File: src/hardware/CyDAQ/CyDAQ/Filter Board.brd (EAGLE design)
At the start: 160.9 x 110.9 mm, 213 parts, among them J1 DCJ0202, J10 Vout_HEADER, J11 5V0_SENSOR, J12 3V3_SENSOR, J13 1V8_SENSOR, J14 BRKOUT_JD, J15 BRKOUT_JC, J16 BRKOUT_JB, J17 BRKOUT_JF, J18 5V0_CONN, J19 3V3_CONN, J2 ZYBO_JF, J20 1V8_CONN, J21 BRKOUT_JD, J22 ZYBO_Power, J3 ZYBO_JE, J4 ZYBO_JD, J5 ZYBO_JC, J6 ZYBO_JB, J7 A_XADC, J8 SJ1-3523N, J9 Vin_HEADER, U1 TPS54531DDARDDA8_3P1X2P4-L, U10 CD74HCT4051, U11 CD74HCT4051, U12 OPA4197, U13 OPA4197, U14 OPA4197, U15 OPA4197, U16 OPA4197, U17 CD74HCT4053, U18 CD74HCT4051, U19 OPA2197, U3 TPS56339, U4 TPS56339, U5 LM43601PWPR, U6 X9258_A, U7 X925_B, U8 X9258_C, U9 X9258_D

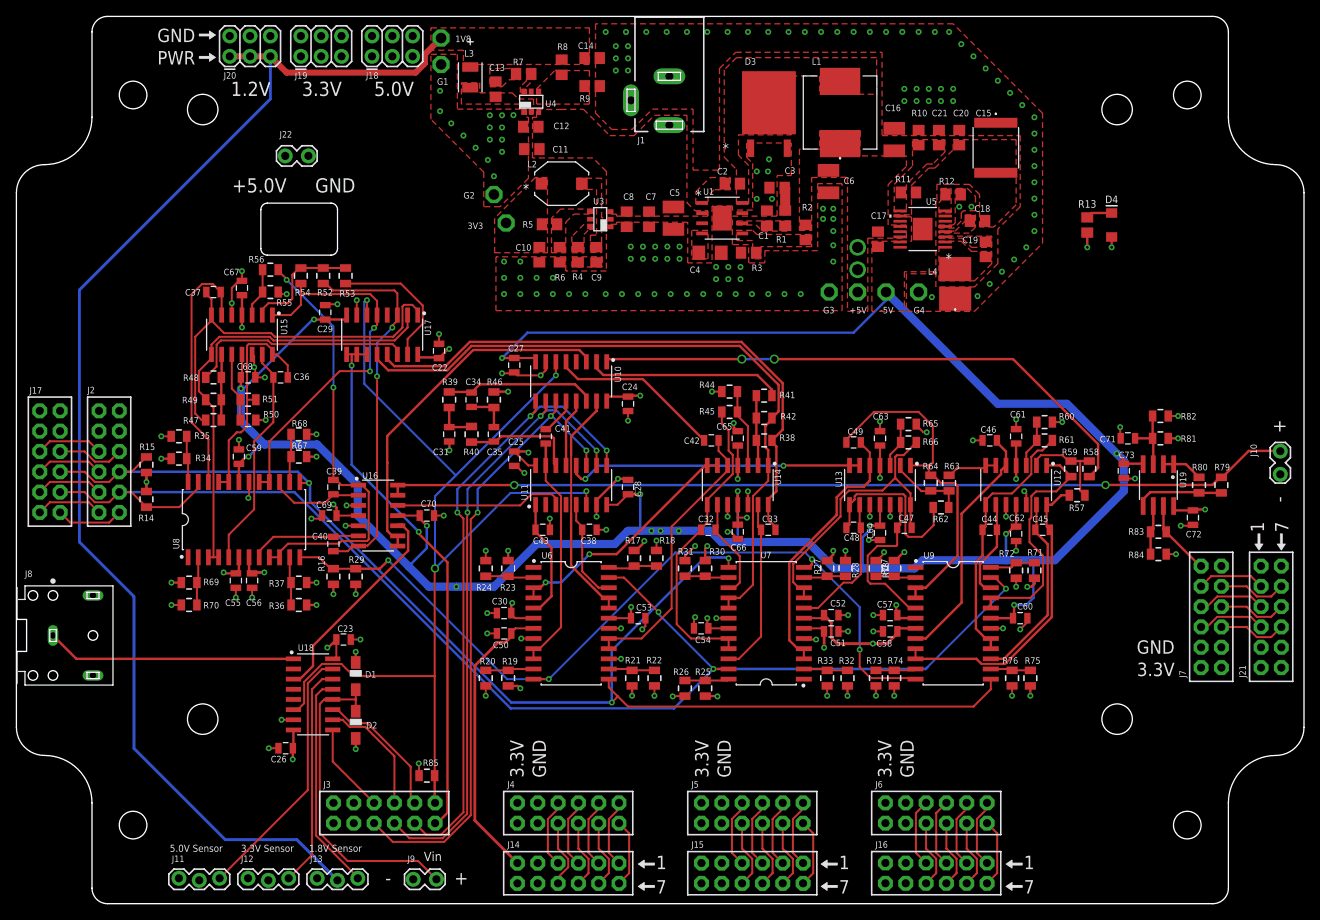
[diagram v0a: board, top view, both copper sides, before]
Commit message: Added silkscreen
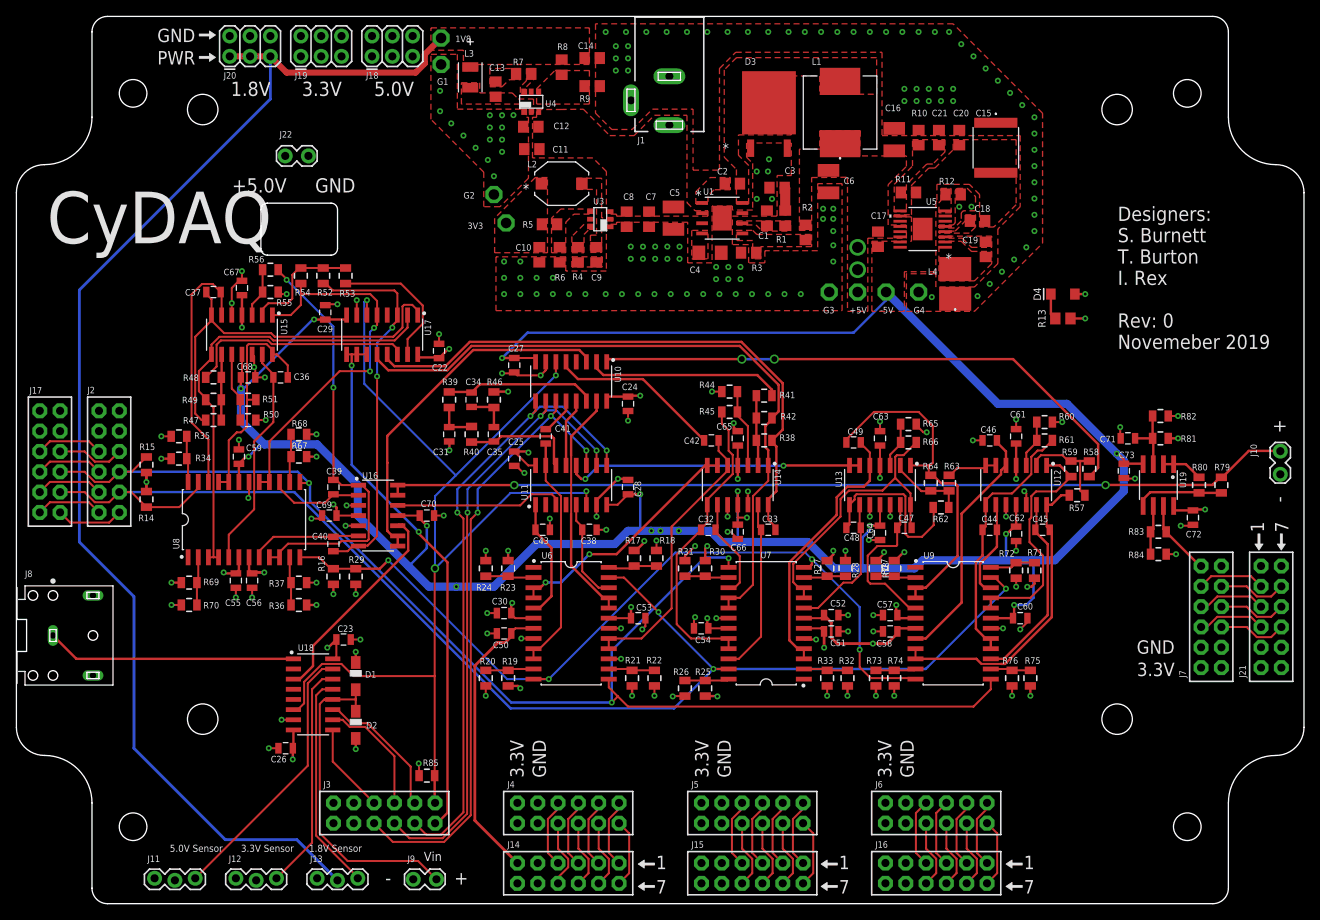
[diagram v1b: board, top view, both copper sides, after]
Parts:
- moved R13 12.1 mm to (130.8, 73.2), turned to 180 degrees
- moved D4 10.6 mm to (130.8, 76.2), turned to 180 degrees
- moved J11 3.05 mm to (17.3, 3.05)
- moved J12 1.52 mm to (27.4, 3.05)
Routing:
- net 5V0SENSOR_IN: track 32.8 -> 34.1 mm
- net 3V3SENSOR_IN: track 27.9 -> 28.6 mm
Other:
- board text added: "1.8V"
- board text added: "CyDAQ"
- board text added: "Designers: S. Burnett T. Burton I. Rex Rev: 0 Novemeber 2019"
- board text removed: "1.2V"

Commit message: Made some final adjustments and added production files
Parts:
- added R43: 10k, Resistors:0805
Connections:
- net 3.5MM_IN: now also J8.2; no longer J8.1
- net GND: now also J8.1, R43.1; no longer J8.2
- net N$73: now also R43.2
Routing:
- net 3.5MM_IN: track 31.3 -> 25.9 mm
- net N$73: track 9.52 -> 14.4 mm
- net GND: track 132.1 -> 133.4 mm, vias 211 -> 212
- net -5V0: track 396.3 -> 395.5 mm
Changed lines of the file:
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@@
 </layers>
 <board>
-<fusionsync huburn="a.cGVyc29uYWw6dWUyZGVhNzMz" projecturn="a.cGVyc29uYWw6dWUyZGVhNzMzIzIwMTkxMTAyMjMzODQwMTI2" f3durn="urn:adsk.wipprod:dm.lineage:zbJ6wBk-RJOF5j4RYDEoYg" pcbguid="4f68e89e-d072-4590-908d-8220ccbcb71c" lastpulledtime="" lastsyncedchangeguid="600b4640-d03a-0c44-81a5-cd04cc5791ac"/>
+<fusionsync huburn="a.cGVyc29uYWw6dWUyZGVhNzMz" projecturn="a.cGVyc29uYWw6dWUyZGVhNzMzIzIwMTkxMTAyMjMzODQwMTI2" f3durn="urn:adsk.wipprod:dm.lineage:zbJ6wBk-RJOF5j4RYDEoYg" pcbguid="4f68e89e-d072-4590-908d-8220ccbcb71c" lastpulledtime="" lastsyncedchangeguid="a0c0b5a2-3287-cb09-0d89-8253cff963cb"/>
 <plain>
 <wire x1="95.489209375" y1="9.88383125" x2="96.089209375" y2="9.88385" width="0.1" layer="51"/>
@@
 <text x="35.687" y="102.743" size="1.778" layer="25" font="vector" ratio="15" rot="R180" align="bottom-right">3.3V</text>
 <text x="44.704" y="102.743" size="1.778" layer="25" font="vector" ratio="15" rot="R180" align="bottom-right">5.0V</text>
-<text x="19.177" y="7.366" size="0.889" layer="25" font="vector" ratio="15" rot="R180" align="bottom-right">5.0V Sensor</text>
-<text x="28.067" y="7.366" size="0.889" layer="25" font="vector" ratio="15" rot="R180" align="bottom-right">3.3V Sensor</text>
-<text x="36.576" y="7.366" size="0.889" layer="25" font="vector" ratio="15" rot="R180" align="bottom-right">1.8V Sensor</text>
+<text x="16.637" y="6.096" size="0.889" layer="25" font="vector" ratio="15" rot="R180" align="bottom-right">5.0V Sensor</text>
+<text x="26.543" y="6.096" size="0.889" layer="25" font="vector" ratio="15" rot="R180" align="bottom-right">3.3V Sensor</text>
+<text x="36.576" y="6.096" size="0.889" layer="25" font="vector" ratio="15" rot="R180" align="bottom-right">1.8V Sensor</text>
 <text x="50.927" y="6.477" size="1.143" layer="25" font="vector" ratio="15" rot="R180" align="bottom-right">Vin</text>
 <text x="54.737" y="4.064" size="1.6764" layer="25" font="vector" ratio="15" rot="R180" align="bottom-right">+</text>
@@
 <attribute name="BOM" value="" x="134.112" y="504.19" size="1.778" layer="27" rot="R270" display="off"/>
 <attribute name="MPN" value="" x="134.112" y="504.19" size="1.778" layer="27" rot="R270" display="off"/>
-<attribute name="NAME" x="77.2795" y="52.832" size="0.8128" layer="25" font="vector" ratio="15" rot="R270"/>
+<attribute name="NAME" x="77.4065" y="52.832" size="0.8128" layer="25" font="vector" ratio="15" rot="R270"/>
 <attribute name="URL" value="" x="134.112" y="504.19" size="1.778" layer="27" rot="R270" display="off"/>
 <attribute name="VALUE" x="75.057" y="53.086" size="0.4064" layer="27" rot="R270"/>
@@
 </element>
 <element name="J11" library="SparkFun-Connectors" library_urn="urn:adsk.eagle:library:513" package="1X03_LOCK" package3d_urn="urn:adsk.eagle:package:38071/1" value="5V0_SENSOR" x="17.272" y="3.048" smashed="yes">
-<attribute name="NAME" x="16.383" y="5.207" size="0.8128" layer="25" font="vector" ratio="15"/>
+<attribute name="NAME" x="14.097" y="4.191" size="0.8128" layer="25" font="vector" ratio="15"/>
 <attribute name="VALUE" x="16.002" y="1.016" size="0.6096" layer="27" font="vector" ratio="20"/>
 </element>
 <element name="J12" library="SparkFun-Connectors" library_urn="urn:adsk.eagle:library:513" package="1X03_LOCK" package3d_urn="urn:adsk.eagle:package:38071/1" value="3V3_SENSOR" x="27.432" y="3.048" smashed="yes">
-<attribute name="NAME" x="26.543" y="5.207" size="0.8128" layer="25" font="vector" ratio="15"/>
+<attribute name="NAME" x="24.511" y="4.191" size="0.8128" layer="25" font="vector" ratio="15"/>
 <attribute name="VALUE" x="26.162" y="1.016" size="0.6096" layer="27" font="vector" ratio="20"/>
 </element>
 <element name="J13" library="SparkFun-Connectors" library_urn="urn:adsk.eagle:library:513" package="1X03_LOCK" package3d_urn="urn:adsk.eagle:package:38071/1" value="1V8_SENSOR" x="37.592" y="3.048" smashed="yes">
-<attribute name="NAME" x="36.703" y="5.207" size="0.8128" layer="25" font="vector" ratio="15"/>
+<attribute name="NAME" x="34.417" y="4.191" size="0.8128" layer="25" font="vector" ratio="15"/>
 <attribute name="VALUE" x="36.322" y="1.016" size="0.6096" layer="27" font="vector" ratio="20"/>
 </element>
@@
 <attribute name="VALUE" x="131.953" y="72.136" size="0.9398" layer="27" font="vector" ratio="15" rot="R180"/>
 </element>
+<element name="R43" library="Resistors" library_urn="urn:adsk.eagle:library:4010572" package="0805" package3d_urn="urn:adsk.eagle:package:4010580/4" value="10k" x="142.748" y="40.894" smashed="yes">
+<attribute name="BOM" value="" x="142.748" y="40.894" size="1.778" layer="27" font="vector" ratio="15" display="off"/>
+<attribute name="MPN" value="" x="142.748" y="40.894" size="1.778" layer="27" font="vector" ratio="15" display="off"/>
+<attribute name="NAME" x="141.986" y="41.7195" size="0.4064" layer="25"/>
+<attribute name="URL" value="" x="142.748" y="40.894" size="1.778" layer="27" font="vector" ratio="15" display="off"/>
+<attribute name="VALUE" x="141.732" y="39.497" size="0.4064" layer="27"/>
+</element>
 </elements>
 <signals>
@@
 <contactref element="J5" pad="3"/>
 <contactref element="J5" pad="4"/>
-<contactref element="J8" pad="2"/>
 <contactref element="J9" pad="1"/>
 <contactref element="J10" pad="2"/>
@@
 <wire x1="131.76" y1="73.152" x2="133.604" y2="73.152" width="0.3048" layer="1"/>
 <via x="133.604" y="73.152" extent="1-16" drill="0.35"/>
+<contactref element="J8" pad="1"/>
+<contactref element="R43" pad="1"/>
+<wire x1="141.773" y1="40.894" x2="140.462" y2="40.894" width="0.254" layer="1"/>
+<via x="140.462" y="40.894" extent="1-16" drill="0.35"/>
 </signal>
 <signal name="N$6">
@@
 <wire x1="60.717" y1="68.21" x2="60.706" y2="68.199" width="0.3048" layer="1"/>
 <via x="60.706" y="68.199" extent="1-16" drill="0.35"/>
-<wire x1="76.454" y1="51.17" x2="77.967" y2="51.17" width="0.3048" layer="1"/>
-<wire x1="77.967" y1="51.17" x2="77.978" y2="51.181" width="0.3048" layer="1"/>
-<via x="77.978" y="51.181" extent="1-16" drill="0.35"/>
+<wire x1="76.454" y1="51.17" x2="76.719" y2="51.17" width="0.3048" layer="1"/>
+<wire x1="76.719" y1="51.17" x2="77.724" y2="50.165" width="0.3048" layer="1"/>
+<via x="77.724" y="50.165" extent="1-16" drill="0.35"/>
 <wire x1="90.17" y1="49.8686" x2="90.17" y2="51.562" width="0.3048" layer="1"/>
 <via x="90.17" y="51.562" extent="1-16" drill="0.35"/>
@@
 <wire x1="82.804" y1="46.609" x2="80.518" y2="46.609" width="1.016" layer="16"/>
 <wire x1="80.518" y1="46.609" x2="79.375" y2="46.609" width="1.016" layer="16"/>
-<wire x1="79.375" y1="46.609" x2="77.978" y2="46.609" width="1.016" layer="16"/>
-<wire x1="77.978" y1="46.609" x2="76.454" y2="46.609" width="1.016" layer="16"/>
+<wire x1="79.375" y1="46.609" x2="77.724" y2="46.609" width="1.016" layer="16"/>
+<wire x1="77.724" y1="46.609" x2="76.454" y2="46.609" width="1.016" layer="16"/>
 <wire x1="65.024" y1="44.958" x2="59.69" y2="39.624" width="1.016" layer="16"/>
 <wire x1="59.69" y1="39.624" x2="54.991" y2="39.624" width="1.016" layer="16"/>
@@
 <wire x1="104.648" y1="71.374" x2="108.712" y2="75.438" width="0.3048" layer="16"/>
 <wire x1="108.712" y1="75.438" x2="108.712" y2="76.454" width="0.3048" layer="16"/>
-<wire x1="77.978" y1="51.181" x2="77.978" y2="46.609" width="0.3048" layer="16"/>
+<wire x1="77.724" y1="50.165" x2="77.724" y2="46.609" width="0.3048" layer="16"/>
 <wire x1="90.17" y1="51.562" x2="90.17" y2="45.212" width="0.3048" layer="16"/>
 <wire x1="106.68" y1="47.244" x2="106.68" y2="46.70259375" width="0.3048" layer="16"/>
@@
 </signal>
 <signal name="3.5MM_IN">
-<wire x1="4.572" y1="33.528" x2="7.493" y2="30.607" width="0.3048" layer="1"/>
-<wire x1="7.493" y1="30.607" x2="34.6286" y2="30.607" width="0.3048" layer="1"/>
-<contactref element="J8" pad="1"/>
 <contactref element="U18" pad="1"/>
+<contactref element="J8" pad="2"/>
+<wire x1="12.192" y1="30.607" x2="34.6286" y2="30.607" width="0.3048" layer="1"/>
+<wire x1="9.572" y1="28.528" x2="11.651" y2="30.607" width="0.254" layer="1"/>
+<wire x1="11.651" y1="30.607" x2="12.192" y2="30.607" width="0.254" layer="1"/>
 </signal>
 <signal name="INPUT_SELECT0">
@@
 <wire x1="147.957540625" y1="42.207184375" x2="143.723" y2="46.441725" width="0.3048" layer="1"/>
 <wire x1="143.723" y1="46.482" x2="143.723" y2="46.441725" width="0.3048" layer="1"/>
-<wire x1="148.084540625" y1="42.207184375" x2="147.957540625" y2="42.207184375" width="0.3048" layer="1"/>
+<wire x1="148.084540625" y1="42.207184375" x2="148.082" y2="42.207184375" width="0.3048" layer="1"/>
+<contactref element="R43" pad="2"/>
+<wire x1="148.082" y1="42.207184375" x2="147.957540625" y2="42.207184375" width="0.3048" layer="1"/>
+<wire x1="143.723" y1="40.894" x2="145.036184375" y2="42.207184375" width="0.254" layer="1"/>
+<wire x1="145.036184375" y1="42.207184375" x2="148.082" y2="42.207184375" width="0.254" layer="1"/>
 </signal>
 <signal name="N$74">
